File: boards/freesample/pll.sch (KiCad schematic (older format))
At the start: 36 parts, among them J13 SMA, J14 SMA, J22 SMA, J23 SMA, U14 LMK04806, U15 ASG-D-V-A-125.000MHZ

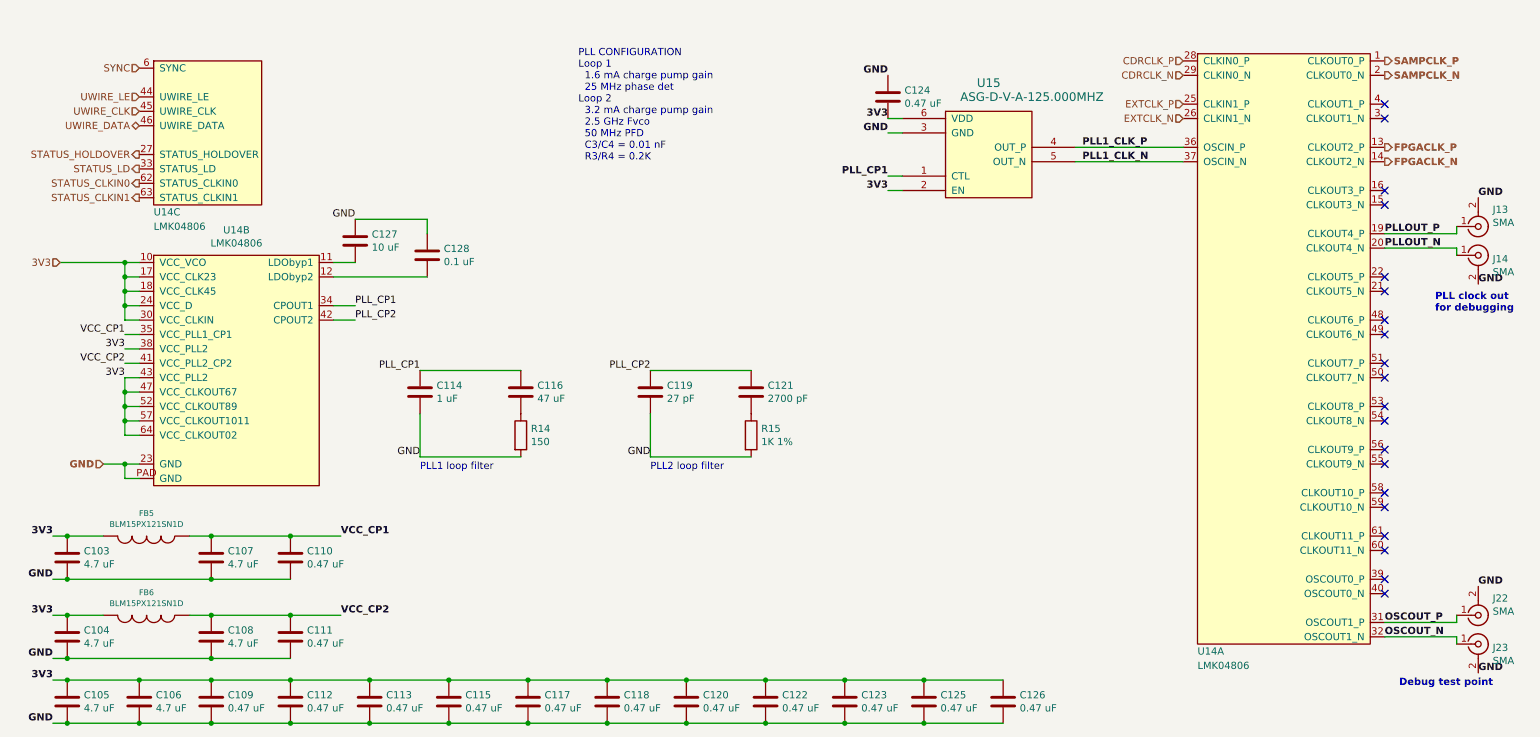
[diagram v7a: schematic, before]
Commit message: Swapped clock inputs to TLK10232 to reduce via count. Began PLL layout.
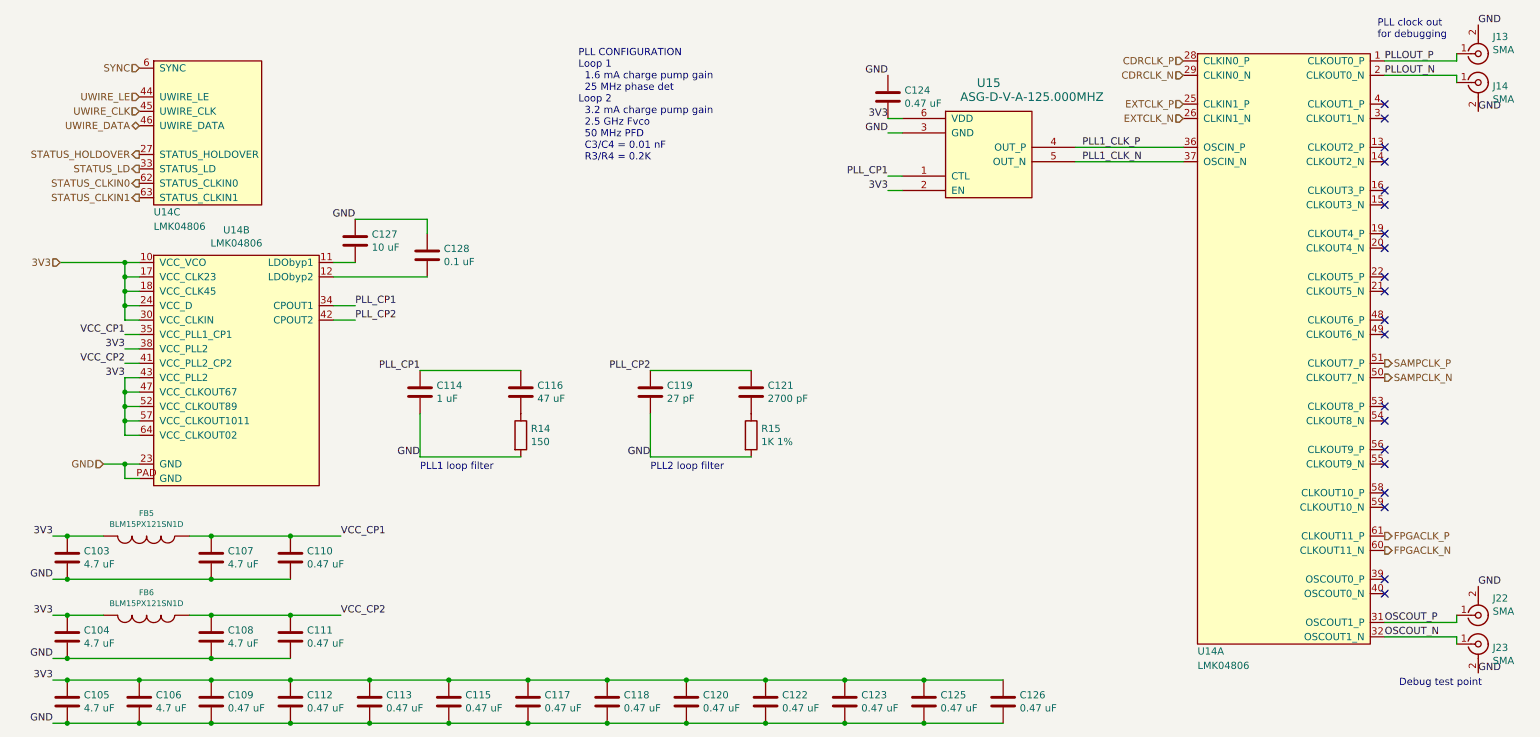
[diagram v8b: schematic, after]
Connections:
- net FPGACLK_N: now also U14.60 (CLKOUT11_N); no longer U14.14 (CLKOUT2_N)
- net FPGACLK_P: now also U14.61 (CLKOUT11_P); no longer U14.13 (CLKOUT2_P)
- net PLLOUT_N: now also U14.2 (CLKOUT0_N); no longer U14.20 (CLKOUT4_N)
- net PLLOUT_P: now also U14.1 (CLKOUT0_P); no longer U14.19 (CLKOUT4_P)
- net SAMPCLK_N: now also U14.50 (CLKOUT7_N); no longer U14.2 (CLKOUT0_N)
- net SAMPCLK_P: now also U14.51 (CLKOUT7_P); no longer U14.1 (CLKOUT0_P)
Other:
- moved on the sheet: J13, J14
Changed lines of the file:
@@
 Sheet 5 12
 Title "FREESAMPLE Oscilloscope"
-Date "2019-03-20"
+Date "2019-03-21"
 Rev "0.1"
 Comp "Andrew D. Zonenberg / Antikernel Labs"
@@
 Text HLabel 1050 2350 0    50   Input ~ 0
 3V3
-Text HLabel 1350 3750 0    50   Input ~ 10
-GND
-Text HLabel 10250 950  2    50   Output ~ 10
+Text HLabel 10250 3050 2    50   Output ~ 0
 SAMPCLK_P
-Text HLabel 10250 1050 2    50   Output ~ 10
+Text HLabel 10250 3150 2    50   Output ~ 0
 SAMPCLK_N
 Text HLabel 1600 1000 0    50   Input ~ 0
@@
 Wire Wire Line
 	1500 3250 1500 3350
-Text Label 3000 4250 0    50   ~ 10
+Text Label 3000 4250 0    50   ~ 0
 VCC_CP1
 $Comp
@@
 Wire Wire Line
 	1100 4250 1350 4250
-Text Label 1000 4250 2    50   ~ 10
+Text Label 1000 4250 2    50   ~ 0
 3V3
 Wire Wire Line
 	1000 4250 1100 4250
 Connection ~ 1100 4250
-Text Label 1000 4550 2    50   ~ 10
+Text Label 1000 4550 2    50   ~ 0
 GND
 Wire Wire Line
@@
 Wire Wire Line
 	2100 4550 1100 4550
-Text Label 3000 4800 0    50   ~ 10
+Text Label 3000 4800 0    50   ~ 0
 VCC_CP2
 $Comp
@@
 Wire Wire Line
 	1100 4800 1350 4800
-Text Label 1000 4800 2    50   ~ 10
+Text Label 1000 4800 2    50   ~ 0
 3V3
 Wire Wire Line
 	1000 4800 1100 4800
 Connection ~ 1100 4800
-Text Label 1000 5100 2    50   ~ 10
+Text Label 1000 5100 2    50   ~ 0
 GND
 Wire Wire Line
@@
 	1    0    0    -1
 $EndComp
-Text Label 1000 5250 2    50   ~ 10
+Text Label 1000 5250 2    50   ~ 0
 3V3
 Wire Wire Line
 	1000 5250 1100 5250
-Text Label 1000 5550 2    50   ~ 10
+Text Label 1000 5550 2    50   ~ 0
 GND
 Wire Wire Line
@@
 Wire Wire Line
 	7050 5550 7600 5550
-NoConn ~ 10250 1250
-NoConn ~ 10250 1350
 NoConn ~ 10250 1850
 NoConn ~ 10250 1950
@@
 NoConn ~ 10250 2750
 NoConn ~ 10250 2850
-NoConn ~ 10250 3050
-NoConn ~ 10250 3150
 NoConn ~ 10250 3350
 NoConn ~ 10250 3450
@@
 NoConn ~ 10250 3950
 NoConn ~ 10250 4050
-NoConn ~ 10250 4250
-NoConn ~ 10250 4350
 NoConn ~ 10250 4550
 NoConn ~ 10250 4650
@@
 Wire Wire Line
 	8850 1650 8100 1650
-Text Label 8150 1550 0    50   ~ 10
+Text Label 8150 1550 0    50   ~ 0
 PLL1_CLK_P
-Text Label 8150 1650 0    50   ~ 10
+Text Label 8150 1650 0    50   ~ 0
 PLL1_CLK_N
-Text Label 6800 1450 2    50   ~ 10
+Text Label 6800 1450 2    50   ~ 0
 GND
 Wire Wire Line
 	6800 1450 6900 1450
-Text Label 6800 1750 2    50   ~ 10
+Text Label 6800 1750 2    50   ~ 0
 PLL_CP1
 Wire Wire Line
 	6800 1750 6900 1750
-Text Label 6800 1850 2    50   ~ 10
+Text Label 6800 1850 2    50   ~ 0
 3V3
 Wire Wire Line
 	6800 1850 6900 1850
-Text Label 6800 1350 2    50   ~ 10
+Text Label 6800 1350 2    50   ~ 0
 3V3
 $Comp
@@
 Wire Wire Line
 	6800 1350 6900 1350
-Text Label 6800 1050 2    50   ~ 10
+Text Label 6800 1050 2    50   ~ 0
 GND
 Text Label 3100 2750 0    50   ~ 0
@@
 	1    0    0    -1
 $EndComp
-Text HLabel 10250 1550 2    50   Output ~ 10
+Text HLabel 10250 4250 2    50   Output ~ 0
 FPGACLK_P
-Text HLabel 10250 1650 2    50   Output ~ 10
+Text HLabel 10250 4350 2    50   Output ~ 0
 FPGACLK_N
 $Comp
 L Connector:Conn_Coaxial J14
 U 1 1 5D284EDA
-P 10900 2300
-F 0 "J14" H 11000 2275 50  0000 L CNN
-F 1 "SMA" H 11000 2184 50  0000 L CNN
-F 2 "azonenberg_pcb:CONN_SMA_EDGE_SAMTEC_SMA_J_P_H_ST_EM1" H 10900 2300 50  0001 C CNN
-F 3 "" H 10900 2300 50  0001 C CNN
-	1    10900 2300
+P 10900 1100
+F 0 "J14" H 11000 1075 50  0000 L CNN
+F 1 "SMA" H 11000 984 50  0000 L CNN
+F 2 "azonenberg_pcb:CONN_SMA_EDGE_SAMTEC_SMA_J_P_H_ST_EM1" H 10900 1100 50  0001 C CNN
+F 3 "" H 10900 1100 50  0001 C CNN
+	1    10900 1100
 	1    0    0    -1
 $EndComp
@@
 L Connector:Conn_Coaxial J13
 U 1 1 5D286A97
-P 10900 2100
-F 0 "J13" H 11000 1982 50  0000 L CNN
-F 1 "SMA" H 11000 2073 50  0000 L CNN
-F 2 "azonenberg_pcb:CONN_SMA_EDGE_SAMTEC_SMA_J_P_H_ST_EM1" H 10900 2100 50  0001 C CNN
-F 3 "" H 10900 2100 50  0001 C CNN
-	1    10900 2100
+P 10900 900
+F 0 "J13" H 11000 782 50  0000 L CNN
+F 1 "SMA" H 11000 873 50  0000 L CNN
+F 2 "azonenberg_pcb:CONN_SMA_EDGE_SAMTEC_SMA_J_P_H_ST_EM1" H 10900 900 50  0001 C CNN
+F 3 "" H 10900 900 50  0001 C CNN
+	1    10900 900
 	1    0    0    1
 $EndComp
 Wire Wire Line
-	10250 2150 10750 2150
-Wire Wire Line
-	10750 2150 10750 2100
-Wire Wire Line
-	10250 2250 10750 2250
-Wire Wire Line
-	10750 2250 10750 2300
-Text Label 10900 1900 0    50   ~ 10
-GND
-Text Label 10900 2500 0    50   ~ 10
-GND
-Text Label 10250 2150 0    50   ~ 10
+	10250 950  10750 950
+Wire Wire Line
+	10750 950  10750 900
+Wire Wire Line
+	10250 1050 10750 1050
+Wire Wire Line
+	10750 1050 10750 1100
+Text Label 10900 700  0    50   ~ 0
+GND
+Text Label 10900 1300 0    50   ~ 0
+GND
+Text Label 10250 950  0    50   ~ 0
 PLLOUT_P
-Text Label 10250 2250 0    50   ~ 10
+Text Label 10250 1050 0    50   ~ 0
 PLLOUT_N
-Text Notes 10600 2700 0    50   ~ 10
+Text Notes 10200 800  0    50   ~ 0
 PLL clock out\nfor debugging
 $Comp
@@
 Wire Wire Line
 	10750 4950 10750 5000
-Text Label 10900 4600 0    50   ~ 10
-GND
-Text Label 10900 5200 0    50   ~ 10
-GND
-Text Label 10250 4850 0    50   ~ 10
+Text Label 10900 4600 0    50   ~ 0
+GND
+Text Label 10900 5200 0    50   ~ 0
+GND
+Text Label 10250 4850 0    50   ~ 0
 OSCOUT_P
-Text Label 10250 4950 0    50   ~ 10
+Text Label 10250 4950 0    50   ~ 0
 OSCOUT_N
-Text Notes 10350 5300 0    50   ~ 10
+Text Notes 10350 5300 0    50   ~ 0
 Debug test point
 Text Label 5150 3700 2    50   ~ 0
@@
 Text Label 3550 3100 2    50   ~ 0
 PLL_CP1
+Text HLabel 1350 3750 0    50   Input ~ 0
+GND
+NoConn ~ 10250 1350
+NoConn ~ 10250 1250
+NoConn ~ 10250 1650
+NoConn ~ 10250 1550
+NoConn ~ 10250 2150
+NoConn ~ 10250 2250
 $EndSCHEMATC
